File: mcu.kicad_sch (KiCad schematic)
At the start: 35 parts, among them IC108 D78C14GF, P101 Conn_01x10, P102 Conn_01x11, P105 Conn_01x11, P107 Conn_01x11, Q105 DTC114EU3

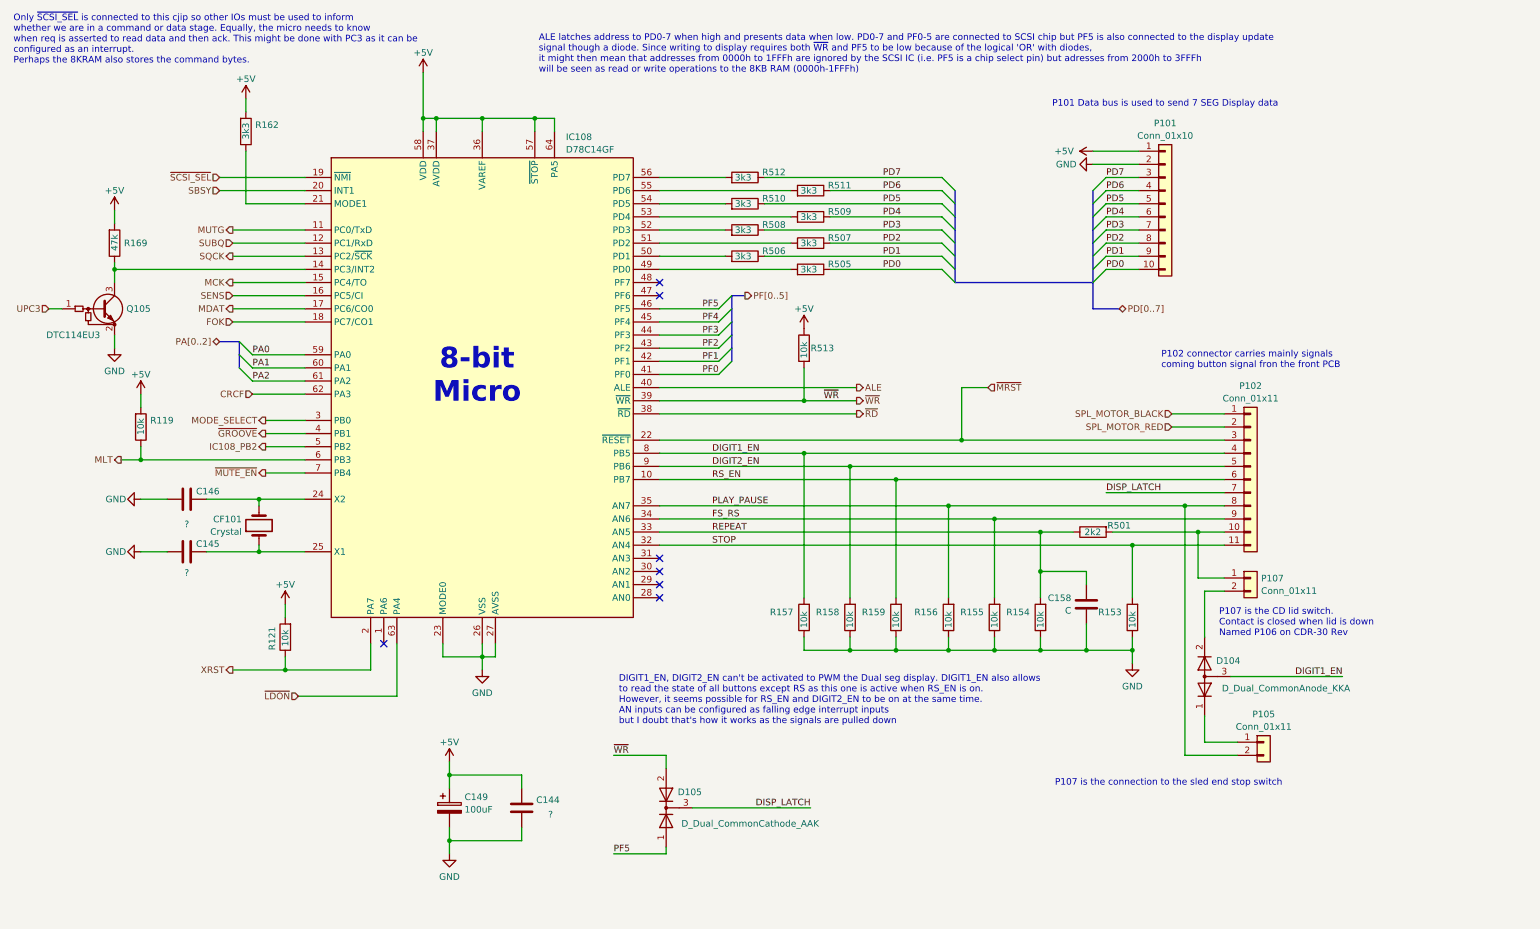
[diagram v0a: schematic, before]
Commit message: Small Schematics update to tidy signals attached to SCSI and MCU chips.
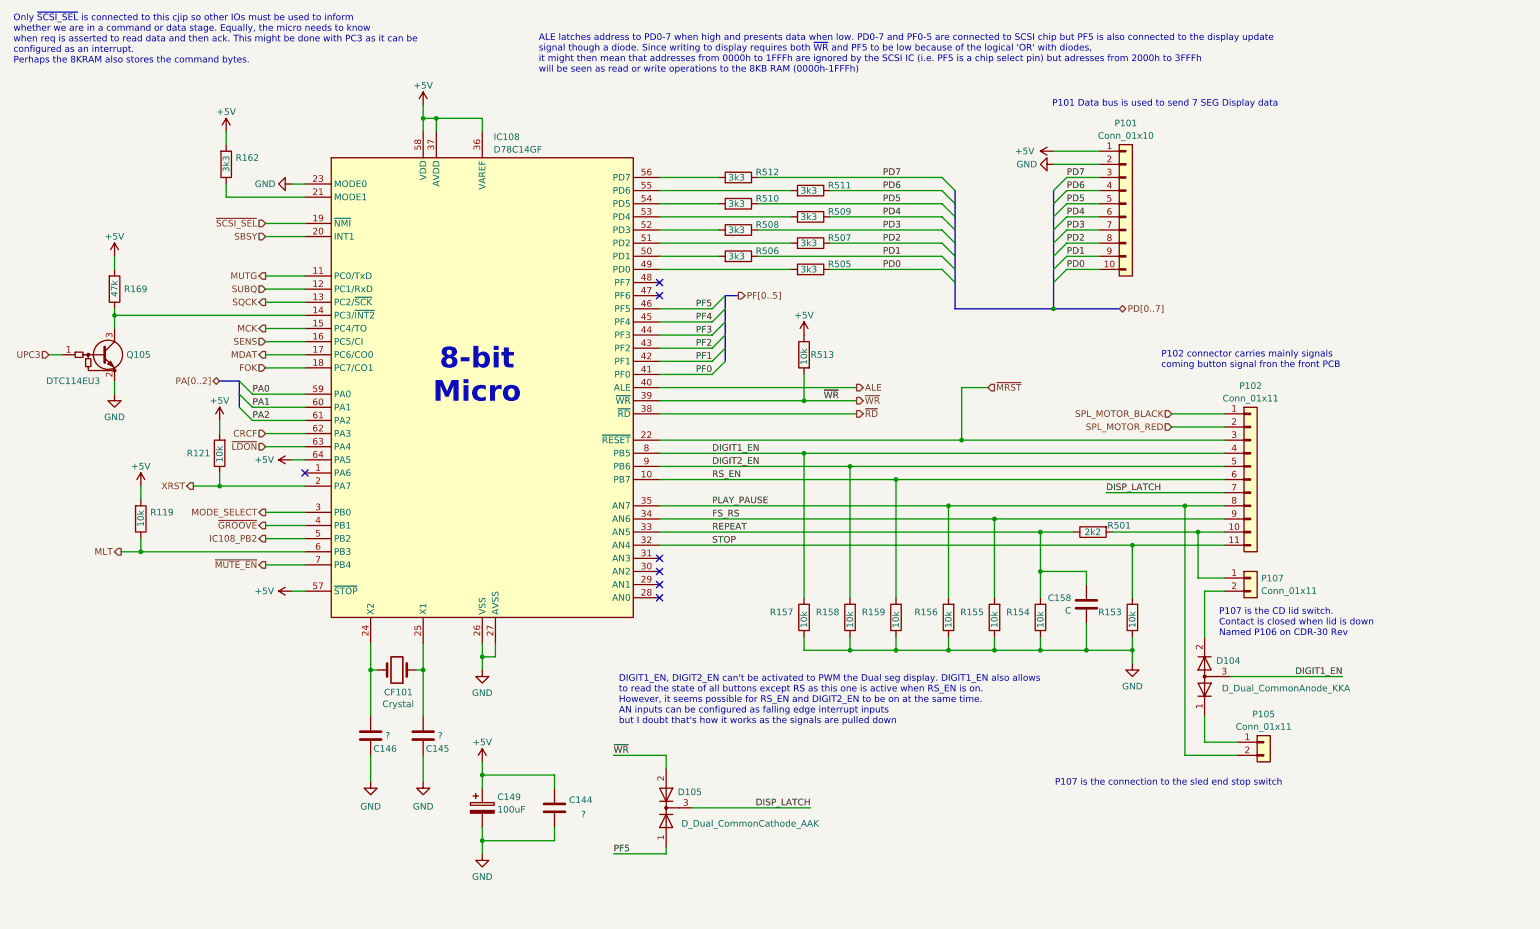
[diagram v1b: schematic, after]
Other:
- moved on the sheet: C144, C145, C146, C149, CF101, P101, Q105, R119, R121, R162, R169, R506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

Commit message: Small update, some typo fixes, more comments added to help understanding
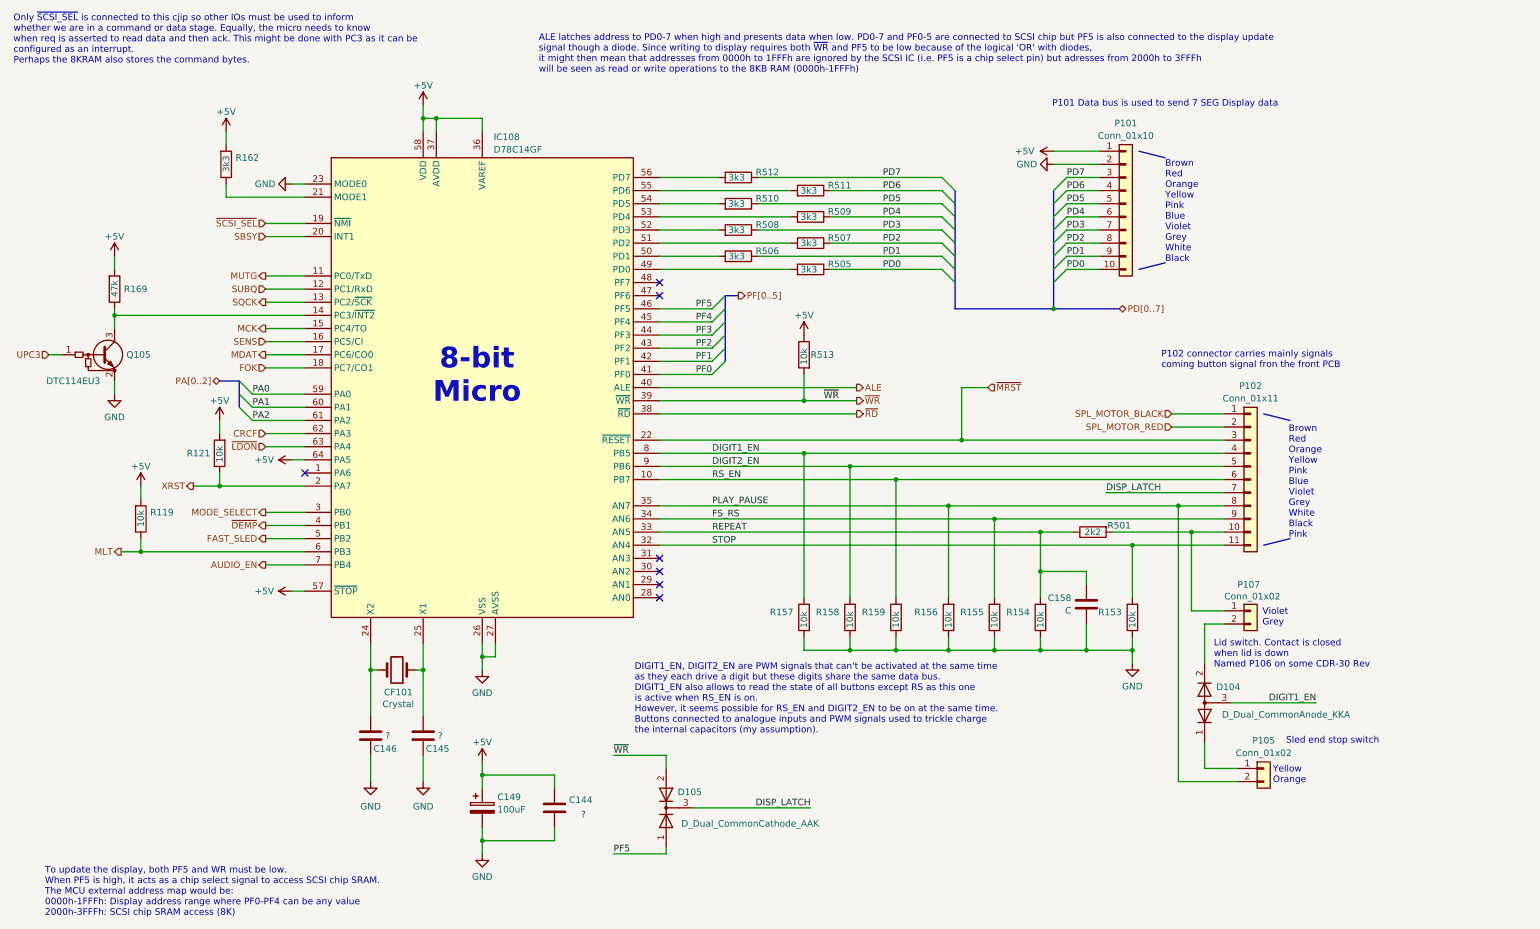
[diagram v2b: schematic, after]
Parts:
- P105, P107: value Conn_01x11 -> Conn_01x02
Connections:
- net IC108_PB2 renamed FAST_SLED
- net ~{GROOVE} renamed ~{DEMP}
- net ~{MUTE_EN} renamed AUDIO_EN
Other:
- note added: "Brown Red Orange Yellow Pink Blue Violet Grey White Black"
- note added: "Brown Red Orange Yellow Pink Blue Violet Grey White Black Pink"
- note added: "DIGIT1_EN, DIGIT2_EN are PWM signals that can't be activated at the same time as they each drive a digit but these digits share the same data bus. DIGIT1_EN also allows to read the state of all buttons except RS as this one is active when RS_EN is on. However, it seems possible for RS_EN and DIGIT2_EN to be on at the same time. Buttons connected to analogue inputs and PWM signals used to trickle 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"
- note added: "Lid switch. Contact is closed when lid is down Named P106 on some CDR-30 Rev"
- note added: "Sled end stop switch"
- note added: "To update the display, both PF5 and WR must be low. When PF5 is high, it acts as a chip select signal to access SCSI chip SRAM. The MCU external address map would be: 0000h-1FFFh: Display address range where PF0-PF4 can be any value 2000h-3FFFh: SCSI chip SRAM access (8K)"
- note added: "Violet Grey"
- note added: "Yellow Orange"
- note removed: "DIGIT1_EN, DIGIT2_EN can't be activated to PWM the Dual seg display. DIGIT1_EN also allows to read the state of all buttons except RS as this one is active when RS_EN is on. However, it seems possible for RS_EN and DIGIT2_EN to be on at the same time. AN inputs can be configured as falling edge interrupt inputs but I doubt that's how it works as the signals are pulled down"
- note removed: "P107 is the CD lid switch. Contact is closed when lid is down Named P106 on CDR-30 Rev"
- note removed: "P107 is the connection to the sled end stop switch"
- moved on the sheet: D104, P105, P107
